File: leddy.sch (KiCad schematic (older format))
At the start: 79 parts, among them J1 hole 1, J2 hole 1, J3 hole 1, J4 hole 1, J5 umbrella support, J6 BARREL_JACK, J7 OPEN HARDWARE, J8 label_power-in, Q1 ZXMP6A13GTA, SW1 SW_DPST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

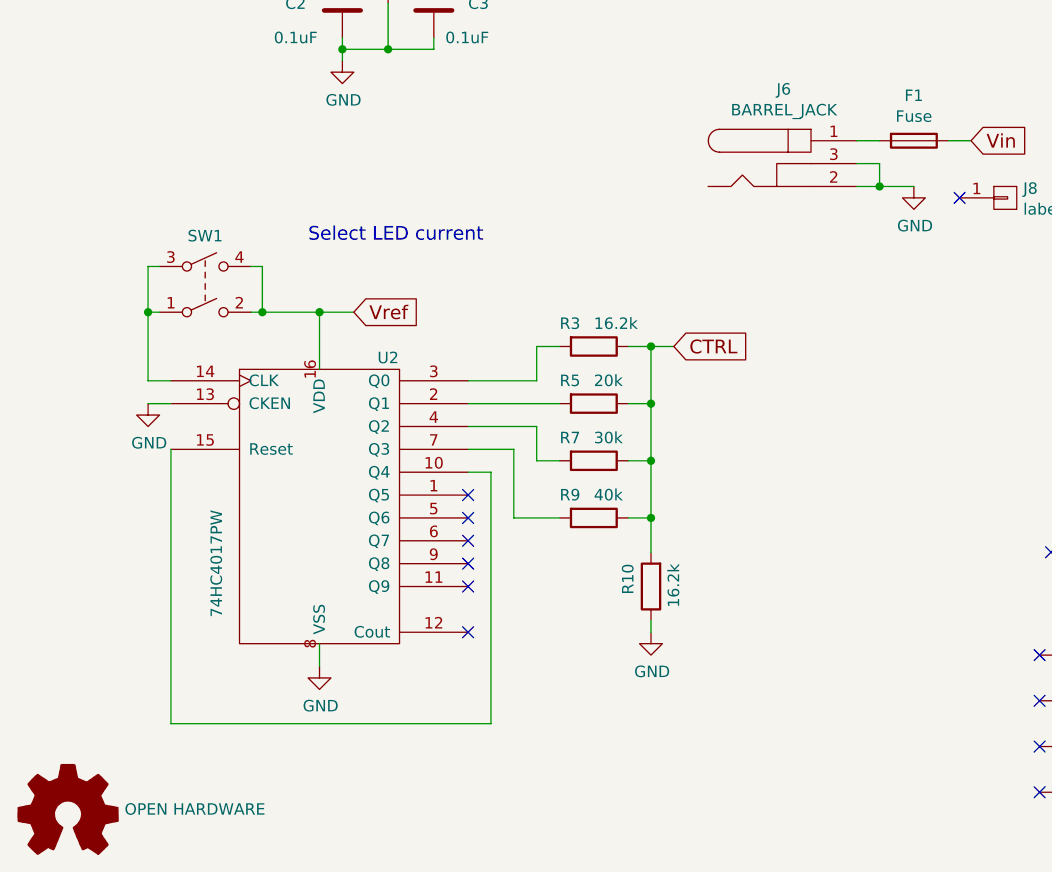
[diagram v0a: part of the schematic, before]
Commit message: added simple debouncing circuit (to be tested)
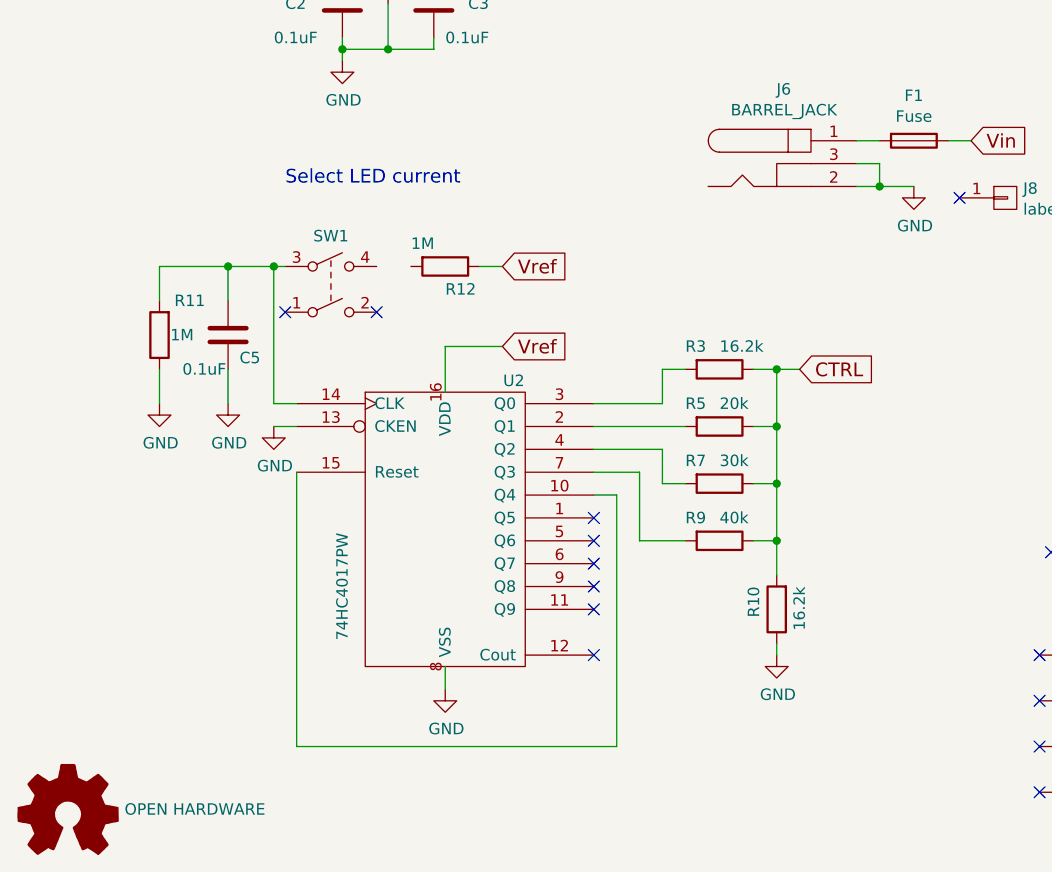
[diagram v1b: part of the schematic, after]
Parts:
- added C5: 0.1uF, Capacitors_SMD:C_0603_HandSoldering, symbol C
- added R11, R12: 1M, Resistors_SMD:R_0603_HandSoldering, symbol R
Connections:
- net GND: now also C5.2, R11.1
- net Vref: now also R12.1; no longer SW1.2, SW1.4
- net at SW1.3, U2.14 (CLK): now also C5.1, R11.2; no longer SW1.1
- no-connect marks 14 -> 16
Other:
- moved on the sheet: R10, R3, R5, R7, R9, SW1, U2

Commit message: started PCB layouting
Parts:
- J5: footprint Mounting_Holes:MountingHole_6.5mm -> Mounting_Holes:MountingHole_8.4mm_M8
- J8: footprint Symbols:Polarity_Center_Positive_6mm_SilkScreen -> lib:Polarity_Center_Positive_3mm_SilkScreen
- SW1: value SW_DPST -> PTS645SM70SMTR92; symbol SW_DPST -> TACT_SW; Description Push button Gull Wing Lead Schurter 1241.1619.11 -> Tactile Switches 50mA 12VDC C&K Components PTS645SM70SMTR92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; SPN1 693-1241.1619.11 -> 611-PTS645SM70SMTR92
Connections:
- net at C5.1, R11.2, U2.14 (CLK): now also SW1.1; no longer SW1.3
- net at SW1.4: now also R12.2
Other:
- note added: "33V, 2A, 1MHz DC/DC BOOST CONVERTER"
- note removed: "1MHz DC/DC BOOST CONVERTER"
- moved on the sheet: C5, R11
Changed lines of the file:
@@
 LIBS:74HC4017PW
 LIBS:logo
+LIBS:tact_switch
 LIBS:leddy-cache
 EELAYER 26 0
@@
 Text Notes 1200 1650 0    60   ~ 0
 VIN=5-28V
-Text Notes 2300 1250 0    60   ~ 0
-1MHz DC/DC BOOST CONVERTER
+Text Notes 1900 1300 0    60   ~ 0
+33V, 2A, 1MHz DC/DC BOOST CONVERTER
 $Comp
 L LED D16
@@
 F 0 "J5" H 5478 6341 50  0000 L CNN
 F 1 "umbrella support" H 5478 6250 50  0000 L CNN
-F 2 "Mounting_Holes:MountingHole_6.5mm" H 5400 6300 50  0001 C CNN
+F 2 "Mounting_Holes:MountingHole_8.4mm_M8" H 5400 6300 50  0001 C CNN
 F 3 "" H 5400 6300 50  0001 C CNN
 F 4 "3.2mm mounting hole" H 5400 6300 60  0001 C CNN "Description"
@@
 	1900 5750 1800 5750
 $Comp
-L SW_DPST SW1
+L TACT_SW SW1
 U 1 1 590B50B8
-P 2050 5150
-F 0 "SW1" H 2050 5383 50  0000 C CNN
-F 1 "SW_DPST" H 2050 5384 50  0001 C CNN
-F 2 "lib:sw_push4p" H 2050 5150 50  0001 C CNN
-F 3 "http://www.mouser.es/ProductDetail/Schurter/1241160111/?qs=%2fha2pyFaduiDEhge8r6YWsU4X%252b6%252b%2fLDTSWv%2fv2zbCGbNuvcoWyyY0A%3d%3d" H 2050 5150 50  0001 C CNN
-F 4 "Push button Gull Wing Lead Schurter 1241.1619.11" H 2050 5150 60  0001 C CNN "Description"
-F 5 "Mouser" H 2050 5150 60  0001 C CNN "SUP1"
-F 6 "693-1241.1619.11" H 2050 5150 60  0001 C CNN "SPN1"
-	1    2050 5150
+P 2100 5150
+F 0 "SW1" H 2100 5383 50  0000 C CNN
+F 1 "PTS645SM70SMTR92" H 2100 5384 50  0001 C CNN
+F 2 "lib:sw_push4p" H 2100 5150 50  0001 C CNN
+F 3 "http://www.mouser.com/ds/2/60/PTS645_7jan16-523842.pdf" H 2100 5150 50  0001 C CNN
+F 4 "Tactile Switches 50mA 12VDC C&K Components PTS645SM70SMTR92 LFS" H 2100 5150 60  0001 C CNN "Description"
+F 5 "Mouser" H 2100 5150 60  0001 C CNN "SUP1"
+F 6 "611-PTS645SM70SMTR92" H 2100 5150 60  0001 C CNN "SPN1"
+	1    2100 5150
 	1    0    0    -1
 $EndComp
@@
 F 0 "J8" H 5078 4791 50  0000 L CNN
 F 1 "label_power-in" H 5078 4700 50  0000 L CNN
-F 2 "Symbols:Polarity_Center_Positive_6mm_SilkScreen" H 5000 4750 50  0001 C CNN
+F 2 "lib:Polarity_Center_Positive_3mm_SilkScreen" H 5000 4750 50  0001 C CNN
 F 3 "" H 5000 4750 50  0001 C CNN
 F 4 "Power in logo" H 5000 4750 60  0001 C CNN "Description"
@@
 L C C5
 U 1 1 590B6942
-P 1600 5350
-F 0 "C5" H 1650 5250 50  0000 L CNN
-F 1 "0.1uF" H 1400 5200 50  0000 L CNN
-F 2 "Capacitors_SMD:C_0603_HandSoldering" H 1638 5200 50  0001 C CNN
-F 3 "" H 1600 5350 50  0001 C CNN
-F 4 "CAP 0.1uF 50V X7R 20% 0603" H 1600 5350 60  0001 C CNN "Description"
-	1    1600 5350
+P 1600 5550
+F 0 "C5" H 1650 5650 50  0000 L CNN
+F 1 "0.1uF" H 1350 5400 50  0000 L CNN
+F 2 "Capacitors_SMD:C_0603_HandSoldering" H 1638 5400 50  0001 C CNN
+F 3 "" H 1600 5550 50  0001 C CNN
+F 4 "CAP 0.1uF 50V X7R 20% 0603" H 1600 5550 60  0001 C CNN "Description"
+	1    1600 5550
 	1    0    0    -1
 $EndComp
@@
 L GND #PWR016
 U 1 1 590B8243
-P 1600 5650
-F 0 "#PWR016" H 1600 5400 50  0001 C CNN
-F 1 "GND" H 1605 5477 50  0000 C CNN
-F 2 "" H 1600 5650 50  0001 C CNN
-F 3 "" H 1600 5650 50  0001 C CNN
-	1    1600 5650
-	1    0    0    -1
-$EndComp
-Wire Wire Line
-	1600 5650 1600 5500
+P 1600 5950
+F 0 "#PWR016" H 1600 5700 50  0001 C CNN
+F 1 "GND" H 1605 5777 50  0000 C CNN
+F 2 "" H 1600 5950 50  0001 C CNN
+F 3 "" H 1600 5950 50  0001 C CNN
+	1    1600 5950
+	1    0    0    -1
+$EndComp
+Wire Wire Line
+	1600 5950 1600 5700
 $Comp
 L R R12
@@
 	0    1    1    0
 $EndComp
-NoConn ~ 2250 5250
-NoConn ~ 1850 5250
 $Comp
 L R R11
 U 1 1 590B99F2
-P 1300 5350
-F 0 "R11" H 1100 5200 50  0000 L CNN
-F 1 "1M" H 1150 5350 50  0000 L CNN
-F 2 "Resistors_SMD:R_0603_HandSoldering" V 1230 5350 50  0001 C CNN
-F 3 "" H 1300 5350 50  0001 C CNN
-F 4 "RES 1M 1% 0603" H 1300 5350 60  0001 C CNN "Description"
-	1    1300 5350
+P 1300 5550
+F 0 "R11" H 1100 5400 50  0000 L CNN
+F 1 "1M" H 1350 5750 50  0000 L CNN
+F 2 "Resistors_SMD:R_0603_HandSoldering" V 1230 5550 50  0001 C CNN
+F 3 "" H 1300 5550 50  0001 C CNN
+F 4 "RES 1M 1% 0603" H 1300 5550 60  0001 C CNN "Description"
+	1    1300 5550
 	-1   0    0    1
 $EndComp
@@
 L GND #PWR017
 U 1 1 590B9D7F
-P 1300 5650
-F 0 "#PWR017" H 1300 5400 50  0001 C CNN
-F 1 "GND" H 1305 5477 50  0000 C CNN
-F 2 "" H 1300 5650 50  0001 C CNN
-F 3 "" H 1300 5650 50  0001 C CNN
-	1    1300 5650
-	1    0    0    -1
-$EndComp
-Wire Wire Line
-	1300 5050 1300 5200
-Wire Wire Line
-	1300 5650 1300 5500
-Wire Wire Line
-	1300 5050 1850 5050
-Wire Wire Line
-	1800 5050 1800 5650
-Wire Wire Line
-	1600 5200 1600 5050
-Connection ~ 1800 5050
-Connection ~ 1600 5050
+P 1300 5950
+F 0 "#PWR017" H 1300 5700 50  0001 C CNN
+F 1 "GND" H 1305 5777 50  0000 C CNN
+F 2 "" H 1300 5950 50  0001 C CNN
+F 3 "" H 1300 5950 50  0001 C CNN
+	1    1300 5950
+	1    0    0    -1
+$EndComp
+Wire Wire Line
+	1300 5950 1300 5700
+Wire Wire Line
+	2400 5050 2300 5050
+Wire Wire Line
+	1300 5250 1900 5250
+Wire Wire Line
+	1600 5250 1600 5400
+Wire Wire Line
+	1300 5400 1300 5250
+Connection ~ 1600 5250
+NoConn ~ 2300 5250
+NoConn ~ 1900 5050
+Wire Wire Line
+	1800 5650 1800 5250
+Connection ~ 1800 5250
 $EndSCHEMATC

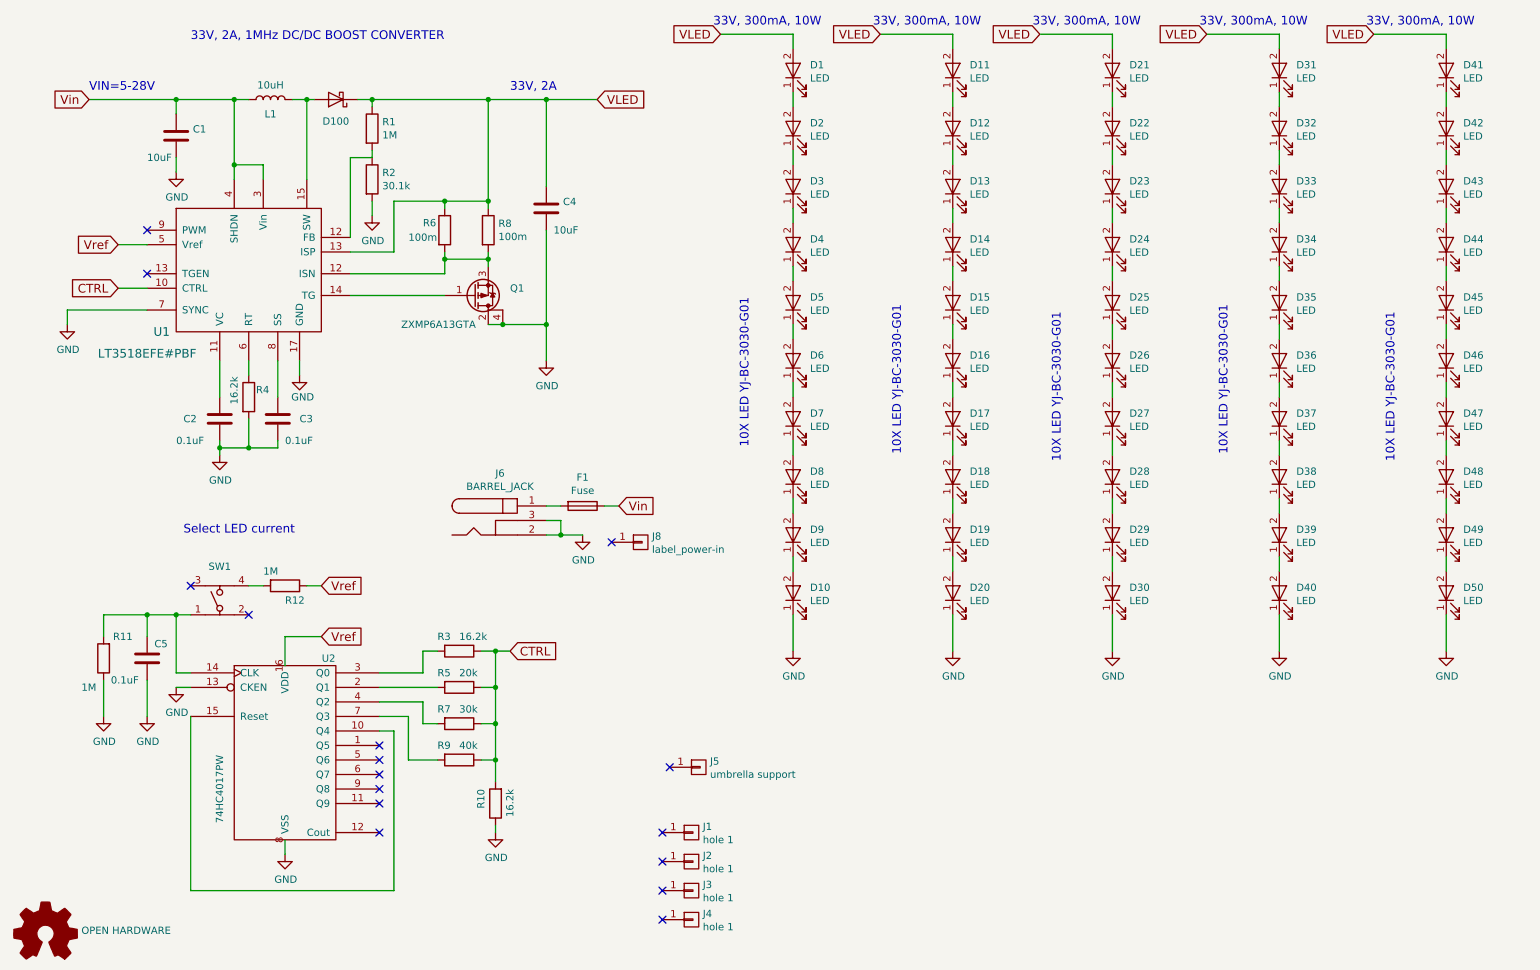
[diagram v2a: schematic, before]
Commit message: added led current level indication
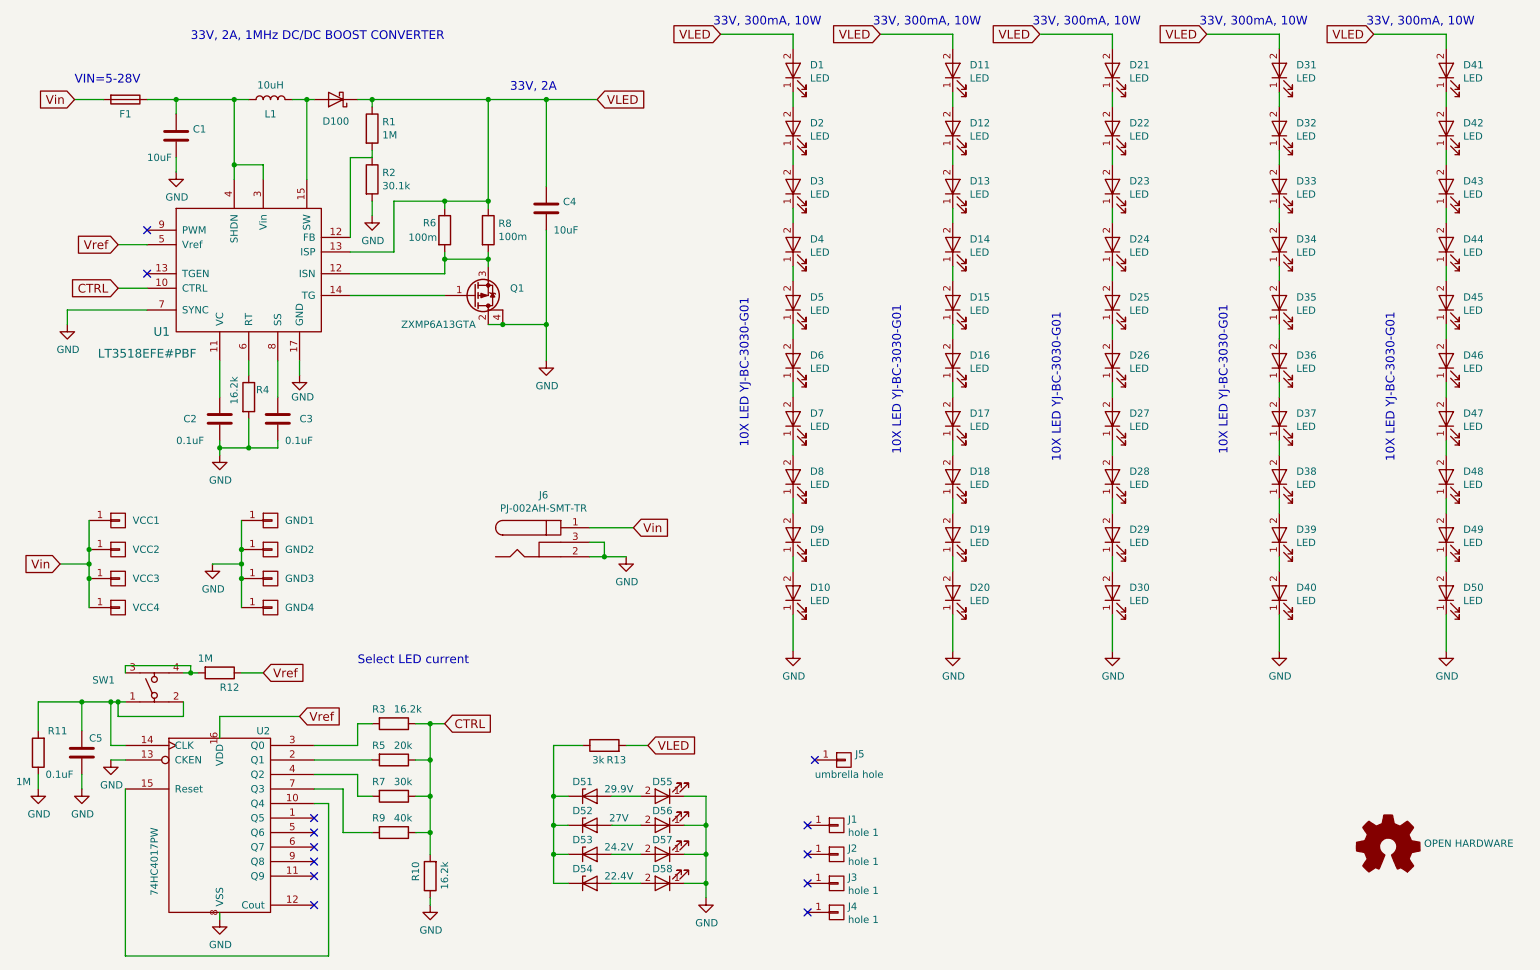
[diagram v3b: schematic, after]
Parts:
- removed J8: label_power-in, lib:Polarity_Center_Positive_3mm_SilkScreen, symbol CONN_01X01
- added D51: 29.9V, Diodes_SMD:D_0603, symbol D_Zener
- added D52: 27V, Diodes_SMD:D_0603, symbol D_Zener
- added D53: 24.2V, Diodes_SMD:D_0603, symbol D_Zener
- added D54: 22.4V, Diodes_SMD:D_0603, symbol D_Zener
- added D55, D56, D57, D58: LED, lib:LED_PLCC-2, symbol LED
- added GND1, GND2, GND3, GND4, VCC1, VCC2, VCC3, VCC4: none, Measurement_Points:Test_Point_Keystone_5019_Minature, symbol CONN_01X01
- added R13: 3k, Resistors_SMD:R_0603_HandSoldering, symbol R
- J5: value umbrella support -> umbrella hole
- J6: value BARREL_JACK -> PJ-002AH-SMT-TR; footprint Connectors:JACK_ALIM -> lib:PJ-002AH-SMT-TR; Description DC in jack connector -> DC in jack connector SMD 2mm, 6,5mm; MAN Switchcraft -> CUI; SPN1 502-RAPC722X -> 490-PJ-002AH-SMT-TR
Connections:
- net GND: now also D55.1 (K), D56.1 (K), D57.1 (K), D58.1 (K), GND1.1 (P1), GND2.1 (P1), GND3.1 (P1), GND4.1 (P1)
- net VLED: now also R13.2
- net Vin: now also F1.2, J6.1, VCC1.1 (P1), VCC2.1 (P1), VCC3.1 (P1), VCC4.1 (P1); no longer C1.1, F1.1, L1.1, U1.3 (Vin), U1.4 (SHDN)
- net at C5.1, R11.2, SW1.1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: now also SW1.2
- net at SW1.3: now also R12.2, SW1.4
- new net: C1.1, F1.1, L1.1, U1.3 (Vin), U1.4 (SHDN)
- new net: D51.1 (K), D52.1 (K), D53.1 (K), D54.1 (K), R13.1
- new net: D51.2 (A), D55.2 (A)
- new net: D52.2 (A), D56.2 (A)
- new net: D53.2 (A), D57.2 (A)
- new net: D54.2 (A), D58.2 (A)
- no-connect marks 16 -> 13
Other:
- moved on the sheet: C5, F1, J1, J2, J3, J4, J5, J6, R10, R11, R12, R3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
